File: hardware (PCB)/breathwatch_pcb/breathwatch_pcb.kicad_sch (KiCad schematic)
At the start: 7 parts, among them J1 Conn_01x08_Socket, J2 Conn_01x08_Socket, J3 Conn_01x04_Socket, J4 USB_A, Q1 AO3401A

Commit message: fixed a few things (PCB, Schematic)
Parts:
- removed J3: Conn_01x04_Socket, Connector_PinHeader_2.54mm:PinHeader_1x04_P2.54mm_Vertical, symbol Connector:Conn_01x04_Socket
- removed J4: USB_A, Connector_USB:USB_A_CNCTech_1001-011-01101_Horizontal, symbol Connector:USB_A
- added J4: Conn_01x08_Socket, Connector_PinSocket_2.54mm:PinSocket_1x08_P2.54mm_Vertical_SMD_Pin1Right, symbol Connector:Conn_01x08_Socket
- added J5: USB_C_Receptacle_PowerOnly_6P, Connector_USB:USB_C_Receptacle_GCT_USB4125-xx-x_6P_TopMnt_Horizontal, symbol Connector:USB_C_Receptacle_PowerOnly_6P
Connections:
- net GND: now also J4.3 (Pin_3), J5.A12 (GND), J5.B12 (GND)
- net at J1.3 (Pin_3): now also J4.5 (Pin_5)
- net at J1.4 (Pin_4): now also J4.4 (Pin_4)
- net at J1.8 (Pin_8): now also J5.A9 (VBUS), J5.B9 (VBUS)
- net at Q1.3 (D): now also J4.2 (Pin_2)

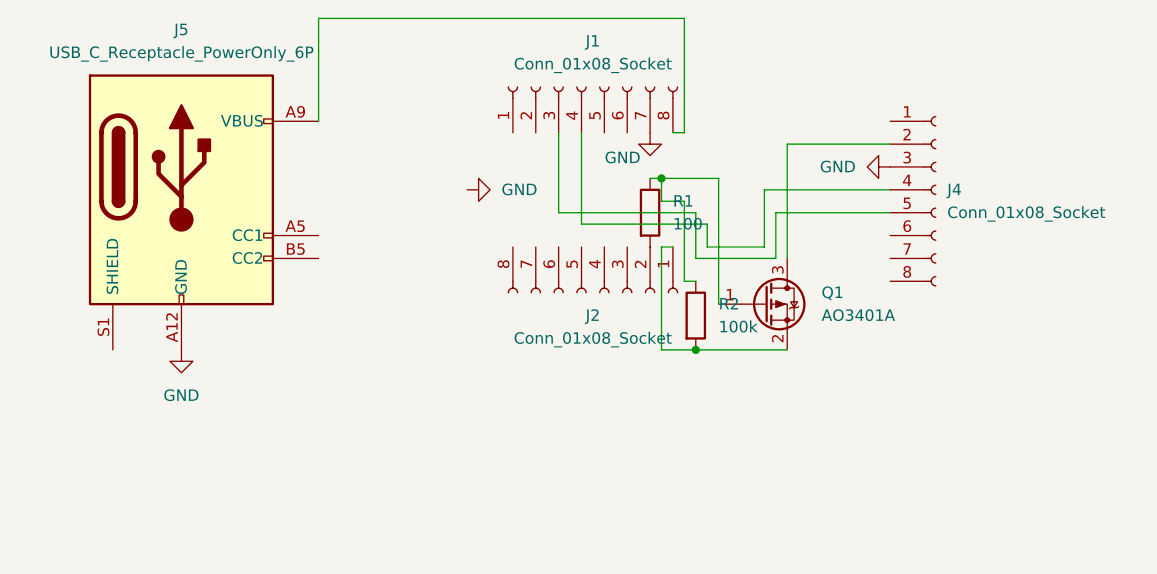
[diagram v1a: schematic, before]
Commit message: added button to PCB
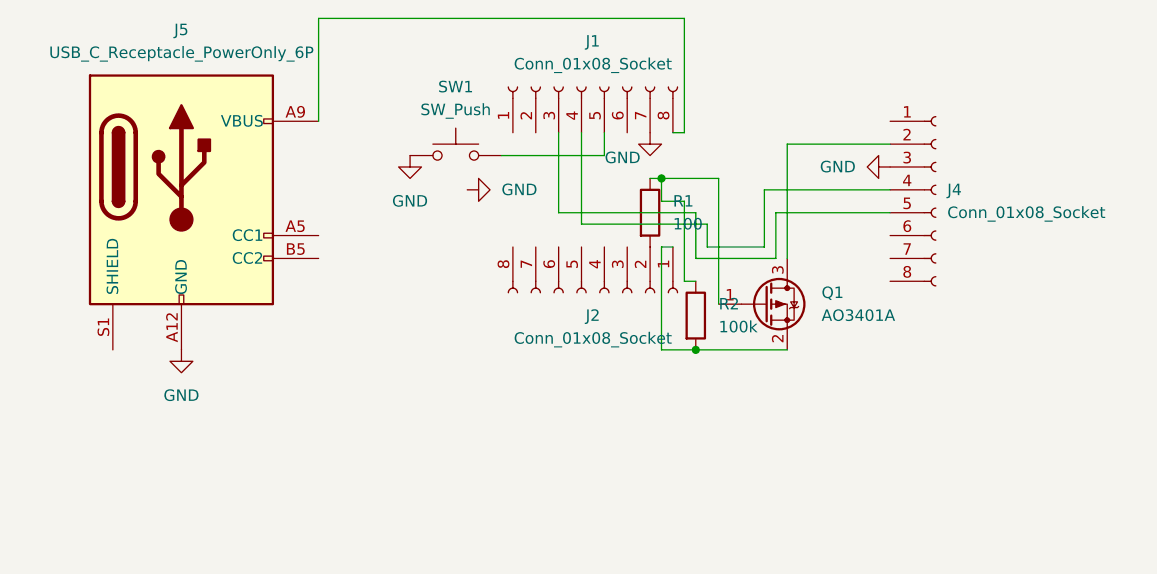
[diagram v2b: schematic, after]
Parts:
- added SW1: SW_Push, Button_Switch_THT:SW_PUSH_6mm_H7.3mm, symbol Switch:SW_Push
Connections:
- net GND: now also SW1.1
- net at J1.5 (Pin_5): now also SW1.2
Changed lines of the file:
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@@
+	(wire
+		(pts
+			(xy 86.36 76.2) (xy 86.36 78.74)
+		)
+		(stroke
+			(width 0)
+			(type default)
+		)
+	)
 	(wire
 		(pts
@@
 		(pts
 			(xy 93.98 76.2) (xy 95.25 76.2)
+		)
+		(stroke
+			(width 0)
+			(type default)
+		)
+	)
+	(wire
+		(pts
+			(xy 74.93 78.74) (xy 86.36 78.74)
 		)
 		(stroke
@@
 	(symbol
 		(lib_id "power:GND")
+		(at 64.77 78.74 0)
+		(unit 1)
+		(exclude_from_sim no)
+		(in_bom yes)
+		(on_board yes)
+		(dnp no)
+		(fields_autoplaced yes)
+		(property "Reference" "#PWR05"
+			(at 64.77 85.09 0)
+			(effects
+				(font
+					(size 1.27 1.27)
+				)
+				(hide yes)
+			)
+		)
+		(property "Value" "GND"
+			(at 64.77 83.82 0)
+			(effects
+				(font
+					(size 1.27 1.27)
+				)
+			)
+		)
+		(property "Footprint" ""
+			(at 64.77 78.74 0)
+			(effects
+				(font
+					(size 1.27 1.27)
+				)
+				(hide yes)
+			)
+		)
+		(property "Datasheet" ""
+			(at 64.77 78.74 0)
+			(effects
+				(font
+					(size 1.27 1.27)
+				)
+				(hide yes)
+			)
+		)
+		(property "Description" "Power symbol creates a global label with name \"GND\" , ground"
+			(at 64.77 78.74 0)
+			(effects
+				(font
+					(size 1.27 1.27)
+				)
+				(hide yes)
+			)
+		)
+		(pin "1"
+		)
+		(instances
+			(project ""
+				(path "/c539da2e-b431-4fd6-89d4-dcd4a3700a5e"
+					(reference "#PWR05")
+					(unit 1)
+				)
+			)
+		)
+	)
+	(symbol
+		(lib_id "power:GND")
 		(at 91.44 76.2 0)
 		(unit 1)
@@
 					(unit 1)
 				)
+			)
+		)
+	)
+	(symbol
+		(lib_id "Switch:SW_Push")
+		(at 69.85 78.74 0)
+		(unit 1)
+		(exclude_from_sim no)
+		(in_bom yes)
+		(on_board yes)
+		(dnp no)
+		(fields_autoplaced yes)
+		(property "Reference" "SW1"
+			(at 69.85 71.12 0)
+			(effects
+				(font
+					(size 1.27 1.27)
+				)
+			)
+		)
+		(property "Value" "SW_Push"
+			(at 69.85 73.66 0)
+			(effects
+				(font
+					(size 1.27 1.27)
+				)
+			)
+		)
+		(property "Footprint" "Button_Switch_THT:SW_PUSH_6mm_H7.3mm"
+			(at 69.85 73.66 0)
+			(effects
+				(font
+					(size 1.27 1.27)
+				)
+				(hide yes)
+			)
+		)
+		(property "Datasheet" "~"
+			(at 69.85 73.66 0)
+			(effects
+				(font
+					(size 1.27 1.27)
+				)
+				(hide yes)
+			)
+		)
+		(property "Description" "Push button switch, generic, two pins"
+			(at 69.85 78.74 0)
+			(effects
+				(font
+					(size 1.27 1.27)
+				)
+				(hide yes)
+			)
+		)
+		(pin "2"
+		)
+		(pin "1"
+		)
+		(instances
+			(project ""
+				(path "/c539da2e-b431-4fd6-89d4-dcd4a3700a5e"
+					(reference "SW1")
+					(unit 1)
+				)

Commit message: added a bit to code
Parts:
- R1, R2: footprint Resistor_THT:R_Axial_DIN0207_L6.3mm_D2.5mm_P7.62mm_Horizontal -> Resistor_SMD:R_0603_1608Metric
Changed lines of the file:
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@@
 			)
 		)
-		(property "Footprint" "Resistor_THT:R_Axial_DIN0207_L6.3mm_D2.5mm_P7.62mm_Horizontal"
+		(property "Footprint" "Resistor_SMD:R_0603_1608Metric"
 			(at 89.662 85.09 90)
 			(effects
@@
 			)
 		)
-		(property "Footprint" "Resistor_THT:R_Axial_DIN0207_L6.3mm_D2.5mm_P7.62mm_Horizontal"
+		(property "Footprint" "Resistor_SMD:R_0603_1608Metric"
 			(at 94.742 96.52 90)
 			(effects

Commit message: PCB Design
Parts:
- removed J1: Conn_01x08_Socket, Connector_PinSocket_2.54mm:PinSocket_1x08_P2.54mm_Vertical_SMD_Pin1Left, symbol Connector:Conn_01x08_Socket
- removed J2: Conn_01x08_Socket, Connector_PinSocket_2.54mm:PinSocket_1x08_P2.54mm_Vertical_SMD_Pin1Right, symbol Connector:Conn_01x08_Socket
- removed J5: USB_C_Receptacle_PowerOnly_6P, Connector_USB:USB_C_Receptacle_GCT_USB4125-xx-x_6P_TopMnt_Horizontal, symbol Connector:USB_C_Receptacle_PowerOnly_6P
- removed Q1: AO3401A, Package_TO_SOT_SMD:SOT-23, symbol Transistor_FET:AO3401A
- removed SW1: SW_Push, Button_Switch_THT:SW_PUSH_6mm_H7.3mm, symbol Switch:SW_Push
- added D1: LED, LED_THT:LED_D5.0mm, symbol Device:LED
- added J1, J2: Conn_01x20_Socket, Connector_PinSocket_2.54mm:PinSocket_1x20_P2.54mm_Vertical, symbol Connector:Conn_01x20_Socket
- added J3: Conn_01x06_Socket, Connector_PinSocket_2.54mm:PinSocket_1x06_P2.54mm_Vertical, symbol Connector:Conn_01x06_Socket
- added Q1: NMOS, Package_TO_SOT_THT:TO-220-3_Vertical, symbol Simulation_SPICE:NMOS
- added R3, R4, R7: 4.7k, Resistor_SMD:R_0815_2038Metric, symbol Device:R
- added R5: 100k, Resistor_SMD:R_0815_2038Metric, symbol Device:R
- added R6, R8: 330, Resistor_SMD:R_0815_2038Metric, symbol Device:R
- added SW1: SW_Push_Dual_x2, Button_Switch_THT:SW_PUSH_6mm_H4.3mm, symbol Switch:SW_Push_Dual_x2
- J4: footprint Connector_PinSocket_2.54mm:PinSocket_1x08_P2.54mm_Vertical_SMD_Pin1Right -> Connector_PinSocket_2.54mm:PinSocket_1x08_P2.54mm_Vertical
- R1: value 100 -> 10k; footprint Resistor_SMD:R_0603_1608Metric -> Resistor_SMD:R_0815_2038Metric
- R2: value 100k -> 20k; footprint Resistor_SMD:R_0603_1608Metric -> Resistor_SMD:R_0815_2038Metric
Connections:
- net GND is gone; now on an unnamed net: J4.3 (Pin_3)
- net at J4.5 (Pin_5): now also J2.6 (Pin_6)
- net at J4.4 (Pin_4): now also J2.7 (Pin_7), R4.2
- net at J4.2 (Pin_2): now also J2.1 (Pin_1)
- net at R1.1, R2.1: now also J3.2 (Pin_2)
- net at R2.2: now also J2.2 (Pin_2), R3.1, R3.2, R4.1
- net at R1.2: now also J2.15 (Pin_15)
- new net: D1.1 (K), J1.2 (Pin_2), Q1.3 (S), R5.2, SW1.1 (C)
- new net: J1.12 (Pin_12), SW1.2 (D)
- new net: J3.4 (Pin_4), Q1.1 (D)
- new net: Q1.2 (G), R5.1, R6.1
- new net: J1.8 (Pin_8), R6.2
- new net: J1.10 (Pin_10), R8.1
- new net: D1.2 (A), R8.2
- new net: J2.13 (Pin_13), R7.1
- new net: J1.1 (Pin_1), J3.5 (Pin_5)
- new net: J3.3 (Pin_3), R7.2
